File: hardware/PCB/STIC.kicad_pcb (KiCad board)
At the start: 2 copper layers, 38 x 80 mm, 12 parts, among them J1 DIP-JST-2P-2.0, J2 Button connector, J3 Laser A, J4 Laser B, Q1 Q_PMOS_GSD, U1 XIAO_BLE, U2 RM3100_Breakout, U3 MDOB048064AV

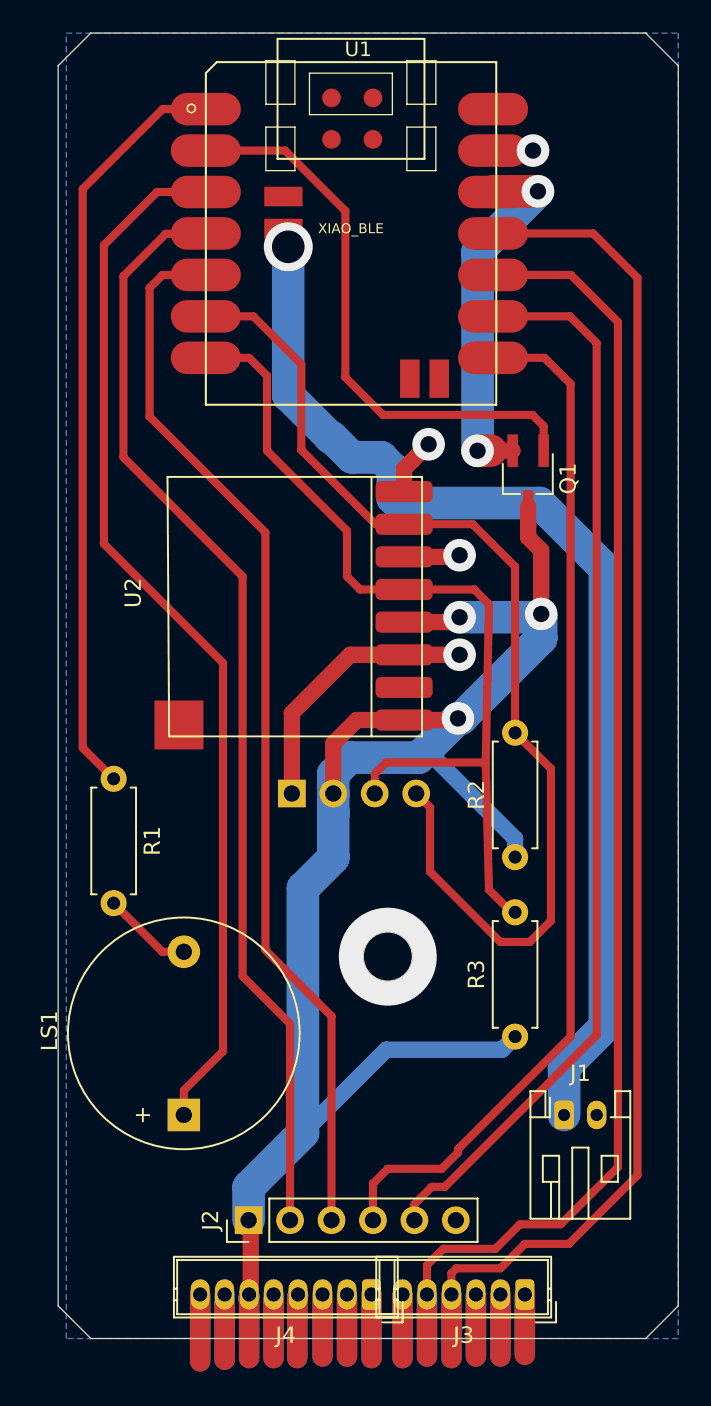
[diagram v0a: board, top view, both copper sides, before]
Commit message: update hardware files, note Button and main board are not connected proper
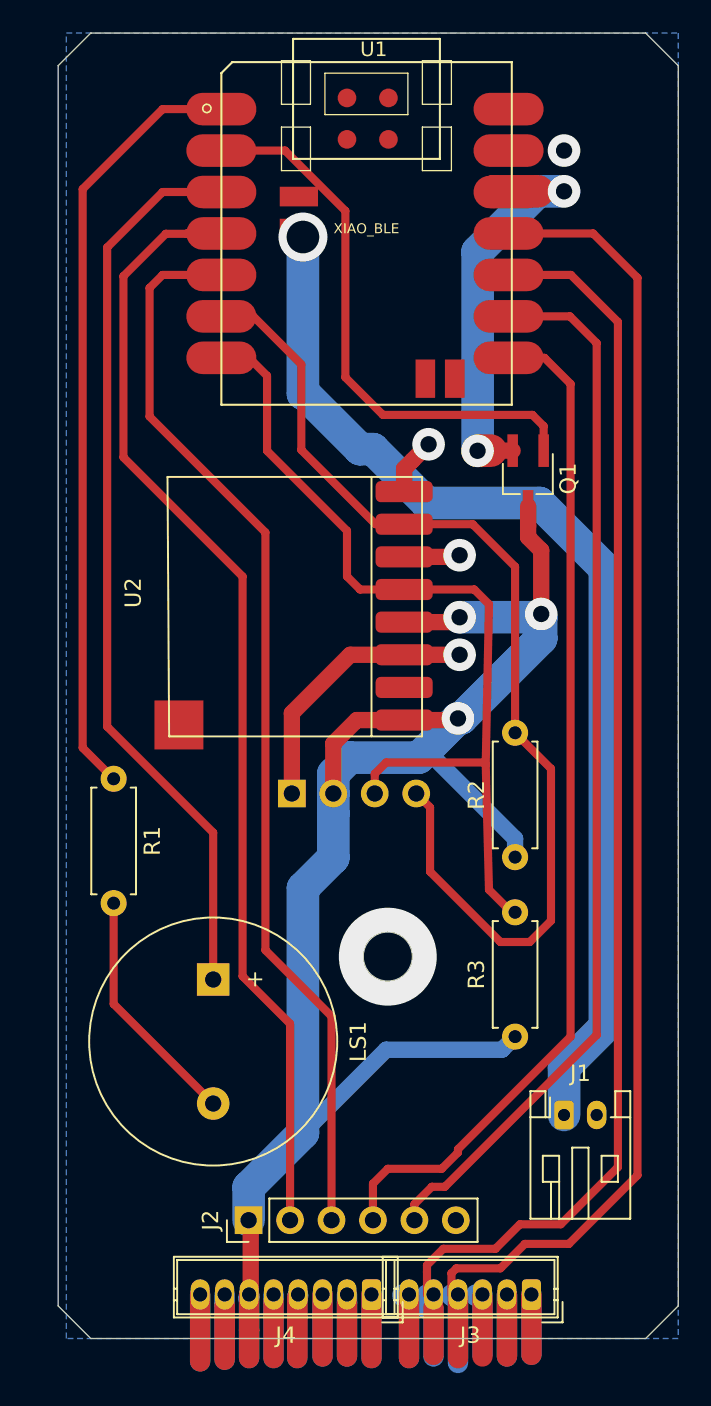
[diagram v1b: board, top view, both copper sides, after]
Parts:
- LS1: footprint Buzzer_Beeper:Buzzer_D14mm_H7mm_P10mm -> Buzzer_Beeper:Buzzer_15x7.5RM7.6
- moved LS1 8.49 mm to (94.2, 116.8), turned to 270 degrees
- moved U1 0.95 mm to (94.8, 81.5)
- moved J3 0.40 mm to (113.8, 136.1)
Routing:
- net Net-(LS1-Pad1): track 64.9 -> 55.0 mm
- net Net-(LS1-Pad2): track 5.53 -> 14.8 mm
- net +BATT: track 68.5 -> 66.6 mm
- net +3.3VA: track 22.4 -> 24.0 mm

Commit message: Fix error in order of pins on button PCB, and other minor PCB fixes
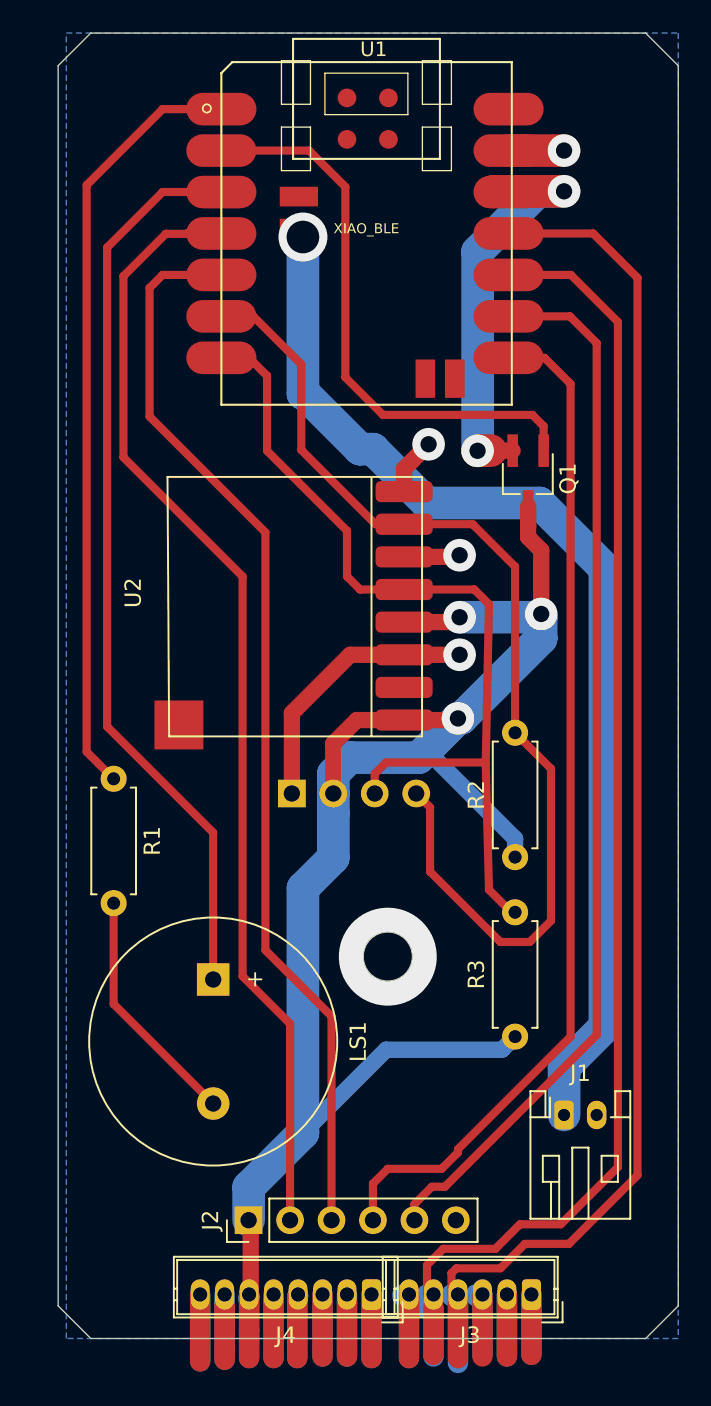
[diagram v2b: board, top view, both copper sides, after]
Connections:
- J2 pad 3: /LED2_R -> /LED2_G
- J2 pad 4: /LED2_G -> /LED2_R
- U1 pad 5: /LED2_R -> /LED2_G
- U1 pad 8: /LED2_G -> /LED2_R
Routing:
- net +3.3VA: track 24.0 -> 27.4 mm
- net GND: track 34.9 -> 38.3 mm
- net /LED2_R: track 65.5 -> 64.2 mm
- net /LED2_G: track 64.2 -> 65.5 mm
- net /PERIPH_EN: track 35.2 -> 36.0 mm
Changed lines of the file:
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@@
     (thickness 1.6)
     (drawings 9)
-    (tracks 218)
+    (tracks 221)
     (zones 0)
     (modules 12)
@@
       (net 8 /BUTTON))
     (pad 5 smd oval (at 0 -7.95782) (size 4.3 1.99898) (layers F.Cu F.Paste F.Mask)
-      (net 7 /LED2_R))
+      (net 6 /LED2_G))
     (pad 6 smd oval (at 0 -5.41782) (size 4.3 1.99898) (layers F.Cu F.Paste F.Mask)
       (net 18 /SDA))
@@
       (net 19 /SCL))
     (pad 8 smd oval (at 17.6 -2.87782) (size 4.3 1.99898) (layers F.Cu F.Paste F.Mask)
-      (net 6 /LED2_G))
+      (net 7 /LED2_R))
     (pad 9 smd oval (at 17.6 -5.41782) (size 4.3 1.99898) (layers F.Cu F.Paste F.Mask)
       (net 5 /LED2_B))
@@
       (net 5 /LED2_B))
     (pad 4 thru_hole oval (at 0 7.62 90) (size 1.7 1.7) (drill 1) (layers *.Cu *.Mask)
-      (net 6 /LED2_G))
-    (pad 3 thru_hole oval (at 0 5.08 90) (size 1.7 1.7) (drill 1) (layers *.Cu *.Mask)
       (net 7 /LED2_R))
+    (pad 3 thru_hole oval (at 0 5.08 90) (size 1.7 1.7) (drill 1) (layers *.Cu *.Mask)
+      (net 6 /LED2_G))
     (pad 2 thru_hole oval (at 0 2.54 90) (size 1.7 1.7) (drill 1) (layers *.Cu *.Mask)
       (net 8 /BUTTON))
@@
   (segment (start 102.65 96.85) (end 105.95 96.85) (width 1) (layer F.Cu) (net 1))
   (segment (start 99.07 100.43) (end 102.65 96.85) (width 1) (layer F.Cu) (net 1))
+  (segment (start 115.75 65.95218) (end 112.35 65.95218) (width 2) (layer F.Cu) (net 1))
   (segment (start 109.25 136.15) (end 109.25 139.95) (width 1.25) (layer F.Cu) (net 2))
   (segment (start 109.15 134.45) (end 108.85 134.75) (width 0.5) (layer F.Cu) (net 2))
@@
   (segment (start 106.58 130.52) (end 107.65 129.45) (width 0.5) (layer F.Cu) (net 5))
   (segment (start 106.58 131.5) (end 106.58 130.52) (width 0.5) (layer F.Cu) (net 5))
-  (segment (start 116.15 80.25) (end 114.55218 78.65218) (width 0.5) (layer F.Cu) (net 6))
-  (segment (start 116.15 120.25) (end 116.15 80.25) (width 0.5) (layer F.Cu) (net 6))
-  (segment (start 109.25 127.35) (end 109.25 127.15) (width 0.5) (layer F.Cu) (net 6))
-  (segment (start 108.25 128.35) (end 109.25 127.35) (width 0.5) (layer F.Cu) (net 6))
-  (segment (start 104.95 128.35) (end 108.25 128.35) (width 0.5) (layer F.Cu) (net 6))
-  (segment (start 109.25 127.15) (end 116.15 120.25) (width 0.5) (layer F.Cu) (net 6))
-  (segment (start 104.04 129.26) (end 104.95 128.35) (width 0.5) (layer F.Cu) (net 6))
-  (segment (start 114.55218 78.65218) (end 110.79768 78.65218) (width 0.5) (layer F.Cu) (net 6))
-  (segment (start 104.04 131.5) (end 104.04 129.26) (width 0.5) (layer F.Cu) (net 6))
-  (segment (start 91.15 73.57218) (end 93.8 73.57218) (width 0.5) (layer F.Cu) (net 7))
-  (segment (start 90.35 74.37218) (end 91.15 73.57218) (width 0.5) (layer F.Cu) (net 7))
-  (segment (start 90.35 82.25) (end 90.35 74.37218) (width 0.5) (layer F.Cu) (net 7))
-  (segment (start 97.45 89.35) (end 90.35 82.25) (width 0.5) (layer F.Cu) (net 7))
-  (segment (start 97.45 114.95) (end 97.45 89.35) (width 0.5) (layer F.Cu) (net 7))
-  (segment (start 101.5 119) (end 97.45 114.95) (width 0.5) (layer F.Cu) (net 7))
-  (segment (start 101.5 131.5) (end 101.5 119) (width 0.5) (layer F.Cu) (net 7))
+  (segment (start 116.15 80.25) (end 114.55218 78.65218) (width 0.5) (layer F.Cu) (net 7))
+  (segment (start 116.15 120.25) (end 116.15 80.25) (width 0.5) (layer F.Cu) (net 7))
+  (segment (start 109.25 127.35) (end 109.25 127.15) (width 0.5) (layer F.Cu) (net 7))
+  (segment (start 108.25 128.35) (end 109.25 127.35) (width 0.5) (layer F.Cu) (net 7))
+  (segment (start 104.95 128.35) (end 108.25 128.35) (width 0.5) (layer F.Cu) (net 7))
+  (segment (start 109.25 127.15) (end 116.15 120.25) (width 0.5) (layer F.Cu) (net 7))
+  (segment (start 104.04 129.26) (end 104.95 128.35) (width 0.5) (layer F.Cu) (net 7))
+  (segment (start 114.55218 78.65218) (end 110.79768 78.65218) (width 0.5) (layer F.Cu) (net 7))
+  (segment (start 104.04 131.5) (end 104.04 129.26) (width 0.5) (layer F.Cu) (net 7))
+  (segment (start 91.15 73.57218) (end 93.8 73.57218) (width 0.5) (layer F.Cu) (net 6))
+  (segment (start 90.35 74.37218) (end 91.15 73.57218) (width 0.5) (layer F.Cu) (net 6))
+  (segment (start 90.35 82.25) (end 90.35 74.37218) (width 0.5) (layer F.Cu) (net 6))
+  (segment (start 97.45 89.35) (end 90.35 82.25) (width 0.5) (layer F.Cu) (net 6))
+  (segment (start 97.45 114.95) (end 97.45 89.35) (width 0.5) (layer F.Cu) (net 6))
+  (segment (start 101.5 119) (end 97.45 114.95) (width 0.5) (layer F.Cu) (net 6))
+  (segment (start 101.5 131.5) (end 101.5 119) (width 0.5) (layer F.Cu) (net 6))
   (segment (start 96.05 116.55) (end 98.96 119.46) (width 0.5) (layer F.Cu) (net 8))
   (segment (start 96.05 92.05) (end 96.05 116.55) (width 0.5) (layer F.Cu) (net 8))
@@
   (segment (start 88.15 118.25) (end 88.15 112.07) (width 0.5) (layer F.Cu) (net 10))
   (segment (start 94.25 124.35) (end 88.15 118.25) (width 0.5) (layer F.Cu) (net 10))
-  (segment (start 98.65218 65.95218) (end 93.8 65.95218) (width 0.5) (layer F.Cu) (net 11))
-  (segment (start 102.35 69.65) (end 98.65218 65.95218) (width 0.5) (layer F.Cu) (net 11))
-  (segment (start 102.35 79.85) (end 102.35 69.65) (width 0.5) (layer F.Cu) (net 11))
-  (segment (start 113.81 82.15) (end 104.65 82.15) (width 0.5) (layer F.Cu) (net 11))
+  (segment (start 100.12618 65.95218) (end 93.8 65.95218) (width 0.5) (layer F.Cu) (net 11))
+  (segment (start 102.35 68.176) (end 100.12618 65.95218) (width 0.5) (layer F.Cu) (net 11))
+  (segment (start 102.35 79.85) (end 102.35 68.176) (width 0.5) (layer F.Cu) (net 11))
   (segment (start 104.65 82.15) (end 102.35 79.85) (width 0.5) (layer F.Cu) (net 11))
+  (segment (start 113.81 82.15) (end 104.65 82.15) (width 0.5) (layer F.Cu) (net 11))
   (segment (start 114.5 82.84) (end 113.81 82.15) (width 0.5) (layer F.Cu) (net 11))
   (segment (start 114.5 84.34) (end 114.5 82.84) (width 0.5) (layer F.Cu) (net 11))
-  (segment (start 91.15 63.41218) (end 86.25 68.31218) (width 0.5) (layer F.Cu) (net 12))
+  (segment (start 86.494 102.794) (end 88.15 104.45) (width 0.5) (layer F.Cu) (net 12))
+  (segment (start 86.494 68.06818) (end 86.494 102.794) (width 0.5) (layer F.Cu) (net 12))
+  (segment (start 91.15 63.41218) (end 86.494 68.06818) (width 0.5) (layer F.Cu) (net 12))
   (segment (start 93.8 63.41218) (end 91.15 63.41218) (width 0.5) (layer F.Cu) (net 12))
-  (segment (start 86.25 102.55) (end 88.15 104.45) (width 0.5) (layer F.Cu) (net 12))
-  (segment (start 86.25 68.31218) (end 86.25 102.55) (width 0.5) (layer F.Cu) (net 12))
   (segment (start 112.75 101.63) (end 112.75 91.45) (width 0.5) (layer F.Cu) (net 18))
   (segment (start 110.15 88.85) (end 105.95 88.85) (width 0.5) (layer F.Cu) (net 18))
@@
   (segment (start 110.45 72.15) (end 114.15 68.45) (width 2) (layer B.Cu) (net 24))
   (segment (start 115.75 68.45) (end 114.15 68.45) (width 2) (layer B.Cu) (net 24))
+  (segment (start 112.39218 68.45) (end 112.35 68.49218) (width 2) (layer F.Cu) (net 24))
+  (segment (start 115.75 68.45) (end 112.39218 68.45) (width 2) (layer F.Cu) (net 24))
   (segment (start 106.25 136.15) (end 106.25 139.95) (width 1.25) (layer F.Cu) (net 25))
   (segment (start 105.85 136.05) (end 105.85 136.15) (width 1.25) (layer B.Cu) (net 25))

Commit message: Convert main pcb to work with egismos laser
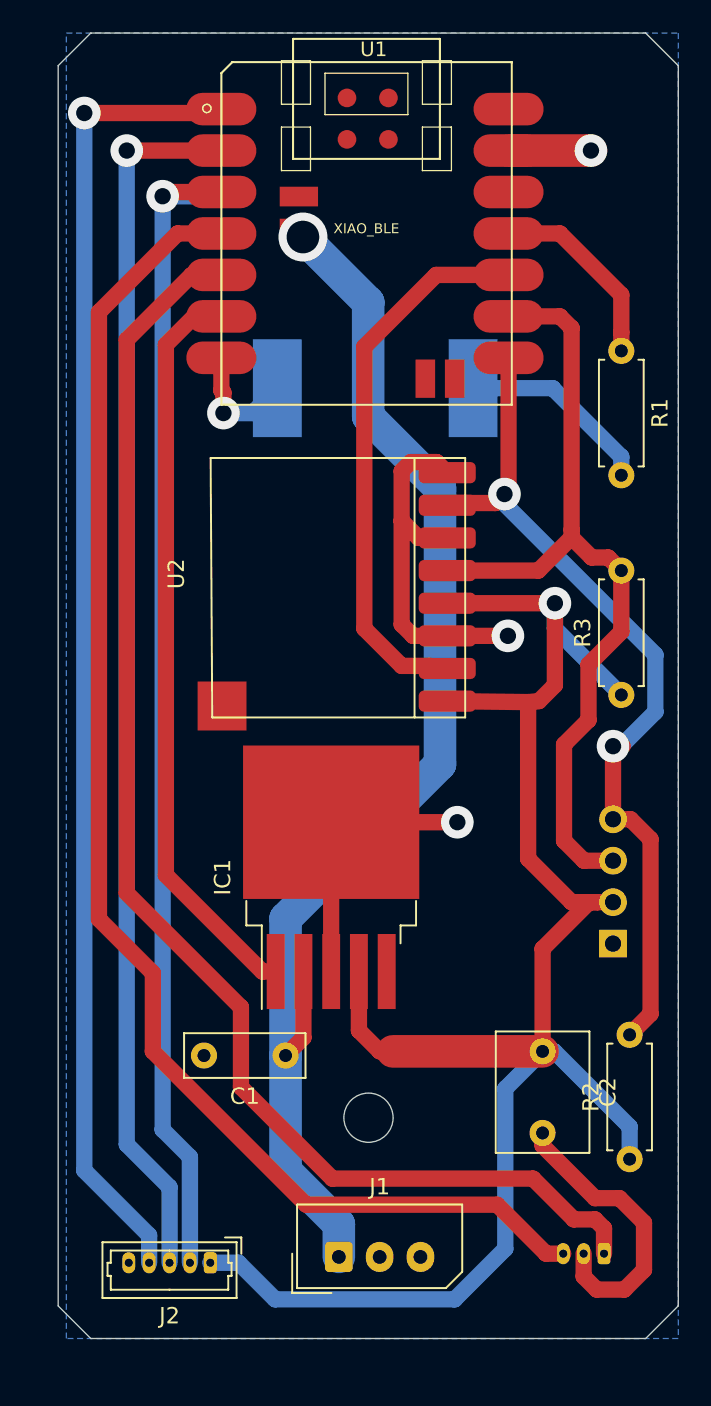
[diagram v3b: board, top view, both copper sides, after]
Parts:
- removed J4: Laser B, Connector_Wuerth:Wuerth_WR-WTB_64800811622_1x08_P1.50mm_Vertical
- removed Q1: Q_PMOS_GSD, Package_TO_SOT_SMD:TSOT-23_HandSoldering
- added C1: 1uF, Capacitor_THT:C_Rect_L7.2mm_W2.5mm_P5.00mm_FKS2_FKP2_MKS2_MKP2, F.Cu at (98.7, 121.4)
- added C2: 47uF, Capacitor_THT:C_Rect_L7.2mm_W5.5mm_P5.00mm_FKS2_FKP2_MKS2_MKP2, F.Cu at (114.4, 121.2)
- added IC1: NCP59301DS33R4G, Package_TO_SOT_SMD:TO-263-5_TabPin6, F.Cu at (101.5, 110.5)
- J1: value DIP-JST-2P-2.0 -> 22-03-5035; footprint Connector_JST:JST_PH_S2B-PH-K_1x02_P2.00mm_Horizontal -> Connector_Molex:Molex_SPOX_5267-03A_1x03_P2.50mm_Vertical
- J2: value Button connector -> 53047-0510; footprint Connector_PinHeader_2.54mm:PinHeader_1x06_P2.54mm_Vertical -> Connector_Molex:Molex_PicoBlade_53047-0510_1x05_P1.25mm_Vertical
- J3: value Laser A -> 53047-0310; footprint Connector_Wuerth:Wuerth_WR-WTB_64800611622_1x06_P1.50mm_Vertical -> Connector_Molex:Molex_PicoBlade_53047-0310_1x03_P1.25mm_Vertical; moved to B.Cu
- LS1: footprint Buzzer_Beeper:Buzzer_15x7.5RM7.6 -> KiCad_imports:SPKR_AST1240MLTRQ; moved to B.Cu
- moved R1 40.7 mm to (119.3, 78.2)
- moved LS1 37.6 mm to (104.2, 80.5), turned to 0 degrees
- moved R3 21.9 mm to (119.3, 99.3)
- moved R2 19.8 mm to (119.8, 127.8)
- moved J1 16.3 mm to (102.0, 133.8)
- moved U3 12.2 mm to (118.8, 106.9), turned to 180 degrees
- moved J3 5.10 mm to (118.2, 133.6)
- moved J2 3.51 mm to (94.1, 134.1), turned to 180 degrees
- moved U2 2.89 mm to (101.9, 92.6)
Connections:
- J1 pad 2: GND -> Net-(J1-Pad2)
- J2 pad 2: /BUTTON -> /Tx
- J2 pad 3: /LED2_G -> /Rx
- J2 pad 4: /LED2_R -> /LASER_EN
- J2 pad 5: /LED2_B -> GND
- J3 pad 1: Net-(J3-Pad1) -> /BUTTON_B
- J3 pad 2: Net-(J3-Pad2) -> GND
- J3 pad 3: Net-(J3-Pad3) -> /BUTTON_A
- LS1 pad 1: Net-(LS1-Pad1) -> /BUZZER_B
- R1 pad 1: Net-(R1-Pad1) -> /BUZZER_A
- U1 pad 1: Net-(R1-Pad1) -> /LASER_EN
- U1 pad 10: /Tx -> /DRDY
- U1 pad 11: /Rx -> /BUZZER_A
- U1 pad 12: +3.3VA -> Net-(U1-Pad12)
- U1 pad 2: /PERIPH_EN -> /Rx
- U1 pad 3: Net-(LS1-Pad1) -> /Tx
- U1 pad 4: /BUTTON -> /BUTTON_A
- U1 pad 5: /LED2_G -> /BUTTON_B
- U1 pad 6: /SDA -> /PERIPH_EN
- U1 pad 7: /SCL -> /BUZZER_B
- U1 pad 8: /LED2_R -> /SDA
- U1 pad 9: /LED2_B -> /SCL
- U2 pad 2: Net-(U2-Pad2) -> /DRDY
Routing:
- net /BUTTON_A: track 0.00 -> 86.4 mm
- net /BUTTON_B: track 0.00 -> 83.5 mm
- net /LASER_EN: track 0.00 -> 80.6 mm, vias 0 -> 1
- net /BUTTON: track 68.2 -> 0.00 mm
- net /LED2_B: track 66.5 -> 0.00 mm
- net /LED2_G: track 65.5 -> 0.00 mm
- net /LED2_R: track 64.2 -> 0.00 mm
- net Net-(LS1-Pad1): track 55.0 -> 0.00 mm
- net Net-(R1-Pad1): track 46.3 -> 0.00 mm
- net /DRDY: track 0.00 -> 34.0 mm
- net +3.3VA: track 27.4 -> 0.00 mm, vias 2 -> 0
- net GND: track 38.3 -> 62.4 mm, vias 4 -> 3
- net /SDA: track 67.1 -> 53.3 mm, vias 0 -> 2
- net /Rx: track 88.5 -> 75.0 mm, vias 0 -> 1
- net /BUZZER_A: track 0.00 -> 11.9 mm
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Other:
- outline, holes or cut-outs redrawn
- rule trace_min: 0.2 -> 0.5
- rule via_min_size: 0.4 -> 0.5
